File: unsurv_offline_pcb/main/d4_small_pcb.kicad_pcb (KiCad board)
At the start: 4 copper layers, 32 x 45 mm, 51 parts, among them Q1 UMH3N, Q2 Q_PMOS_GSD, U1 TTGO-Micro32-ESP32, U2 MCP73831-2-OT, U3 CAM-M8C-0-10, U4 AP2112K-3.3, U5 CH340G, U6 RF430CL330H, U7 BMA400-I2C

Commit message: d4 case updates
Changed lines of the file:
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@@
     (uvia_drill 0.1)
+  )
+  (module unsurv_offline_pcb_footprints:BMA400 (layer F.Cu)
+    (at 44.9 50.5)
+    (fp_text reference U7 (at 2.9 0) (layer F.SilkS)
+      (effects (font (size 0.4 0.4) (thickness 0.08)))
+    )
+    (fp_text value BMA400-I2C (at 0 2.1) (layer F.Fab)
+      (effects (font (size 1 1) (thickness 0.15)))
+    )
+    (fp_circle (center -1.55 -1.07) (end -1.64 -0.96) (layer F.SilkS) (width 0.12))
+    (fp_line (start -1 1) (end 1 1) (layer F.SilkS) (width 0.12))
+    (fp_line (start -1 -1) (end -1 1) (layer F.SilkS) (width 0.12))
+    (fp_line (start 1 -1) (end -1 -1) (layer F.SilkS) (width 0.12))
+    (fp_line (start 1 1) (end 1 -1) (layer F.SilkS) (width 0.12))
+    (pad 11 smd rect (at 0.25 -0.9 270) (size 0.6 0.28) (layers F.Cu F.Paste F.Mask)
+      (net 34 "Net-(U7-Pad11)"))
+    (pad 12 smd rect (at -0.25 -0.9 270) (size 0.6 0.28) (layers F.Cu F.Paste F.Mask)
+      (net 23 SCL))
+    (pad 10 smd rect (at 0.9 -0.75 180) (size 0.6 0.28) (layers F.Cu F.Paste F.Mask)
+      (net 7 +3V3))
+    (pad 9 smd rect (at 0.9 -0.25 180) (size 0.6 0.28) (layers F.Cu F.Paste F.Mask)
+      (net 4 GND))
+    (pad 8 smd rect (at 0.9 0.25 180) (size 0.6 0.28) (layers F.Cu F.Paste F.Mask)
+      (net 4 GND))
+    (pad 7 smd rect (at 0.9 0.75 180) (size 0.6 0.28) (layers F.Cu F.Paste F.Mask)
+      (net 7 +3V3))
+    (pad 6 smd rect (at 0.25 0.9 90) (size 0.6 0.28) (layers F.Cu F.Paste F.Mask)
+      (net 27 ACC_INT2))
+    (pad 5 smd rect (at -0.25 0.9 90) (size 0.6 0.28) (layers F.Cu F.Paste F.Mask)
+      (net 26 ACC_INT1))
+    (pad 4 smd rect (at -0.9 0.75) (size 0.6 0.28) (layers F.Cu F.Paste F.Mask)
+      (net 81 "Net-(U7-Pad4)"))
+    (pad 3 smd rect (at -0.9 0.25) (size 0.6 0.28) (layers F.Cu F.Paste F.Mask)
+      (net 7 +3V3))
+    (pad 2 smd rect (at -0.9 -0.25) (size 0.6 0.28) (layers F.Cu F.Paste F.Mask)
+      (net 22 SDA))
+    (pad 1 smd rect (at -0.9 -0.75) (size 0.6 0.28) (layers F.Cu F.Paste F.Mask)
+      (net 4 GND))
   )
   (module unsurv_offline_pcb_footprints:TF-SMD_TF-101B (layer F.Cu)
@@
     )
   )
-  (module unsurv_offline_pcb_footprints:BMA400 (layer F.Cu)
-    (at 44.9 50.5)
-    (fp_text reference U7 (at 2.9 0) (layer F.SilkS)
-      (effects (font (size 0.4 0.4) (thickness 0.08)))
-    )
-    (fp_text value BMA400-I2C (at 0 2.1) (layer F.Fab)
-      (effects (font (size 1 1) (thickness 0.15)))
-    )
-    (fp_line (start 1 1) (end 1 -1) (layer F.SilkS) (width 0.12))
-    (fp_line (start 1 -1) (end -1 -1) (layer F.SilkS) (width 0.12))
-    (fp_line (start -1 -1) (end -1 1) (layer F.SilkS) (width 0.12))
-    (fp_line (start -1 1) (end 1 1) (layer F.SilkS) (width 0.12))
-    (pad 1 smd rect (at -0.9 -0.75) (size 0.6 0.28) (layers F.Cu F.Paste F.Mask)
-      (net 4 GND))
-    (pad 2 smd rect (at -0.9 -0.25) (size 0.6 0.28) (layers F.Cu F.Paste F.Mask)
-      (net 22 SDA))
-    (pad 3 smd rect (at -0.9 0.25) (size 0.6 0.28) (layers F.Cu F.Paste F.Mask)
-      (net 7 +3V3))
-    (pad 4 smd rect (at -0.9 0.75) (size 0.6 0.28) (layers F.Cu F.Paste F.Mask)
-      (net 81 "Net-(U7-Pad4)"))
-    (pad 5 smd rect (at -0.25 0.9 90) (size 0.6 0.28) (layers F.Cu F.Paste F.Mask)
-      (net 26 ACC_INT1))
-    (pad 6 smd rect (at 0.25 0.9 90) (size 0.6 0.28) (layers F.Cu F.Paste F.Mask)
-      (net 27 ACC_INT2))
-    (pad 7 smd rect (at 0.9 0.75 180) (size 0.6 0.28) (layers F.Cu F.Paste F.Mask)
-      (net 7 +3V3))
-    (pad 8 smd rect (at 0.9 0.25 180) (size 0.6 0.28) (layers F.Cu F.Paste F.Mask)
-      (net 4 GND))
-    (pad 9 smd rect (at 0.9 -0.25 180) (size 0.6 0.28) (layers F.Cu F.Paste F.Mask)
-      (net 4 GND))
-    (pad 10 smd rect (at 0.9 -0.75 180) (size 0.6 0.28) (layers F.Cu F.Paste F.Mask)
-      (net 7 +3V3))
-    (pad 12 smd rect (at -0.25 -0.9 270) (size 0.6 0.28) (layers F.Cu F.Paste F.Mask)
-      (net 23 SCL))
-    (pad 11 smd rect (at 0.25 -0.9 270) (size 0.6 0.28) (layers F.Cu F.Paste F.Mask)
-      (net 34 "Net-(U7-Pad11)"))
-  )
   (module Package_SO:SOIC-16_3.9x9.9mm_P1.27mm (layer F.Cu)

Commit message: small updates to PCB and case
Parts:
- removed JP2: SolderJumper_2_Open, Jumper:SolderJumper-2_P1.3mm_Open_RoundedPad1.0x1.5mm
- C3: value 2.2yF -> 4.7yF
- moved S2 0.20 mm to (34.7, 55.7)
- renumbered + to BATT+1, - to BATT-1
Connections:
- R4 pad 1: Net-(JP2-Pad1) -> +3V3
- R5 pad 1: Net-(JP2-Pad1) -> +3V3
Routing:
- net Net-(JP2-Pad1): track 6.34 -> 0.00 mm, vias 1 -> 0
- net +3V3: track 58.9 -> 60.3 mm
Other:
- board text removed: "I2C 3.3k Pullups"

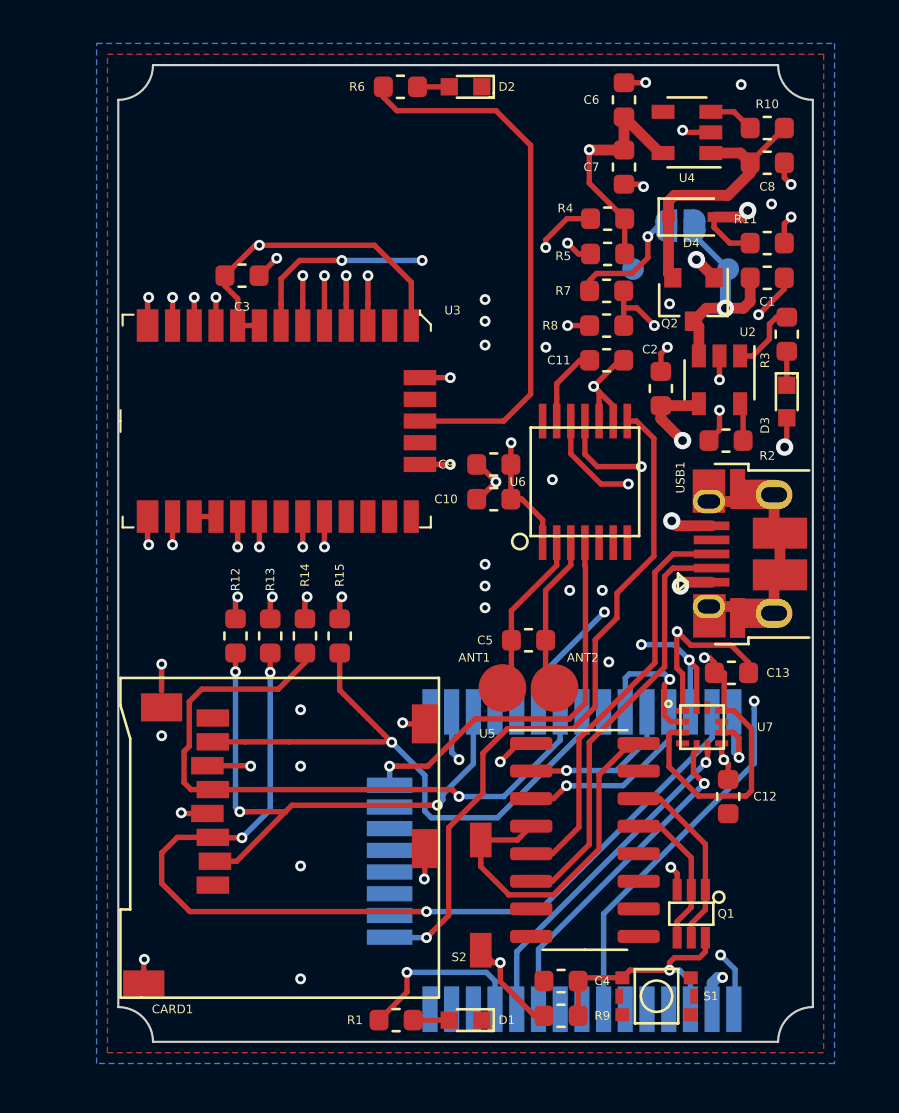
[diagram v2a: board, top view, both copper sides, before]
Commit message: added expansion and JST
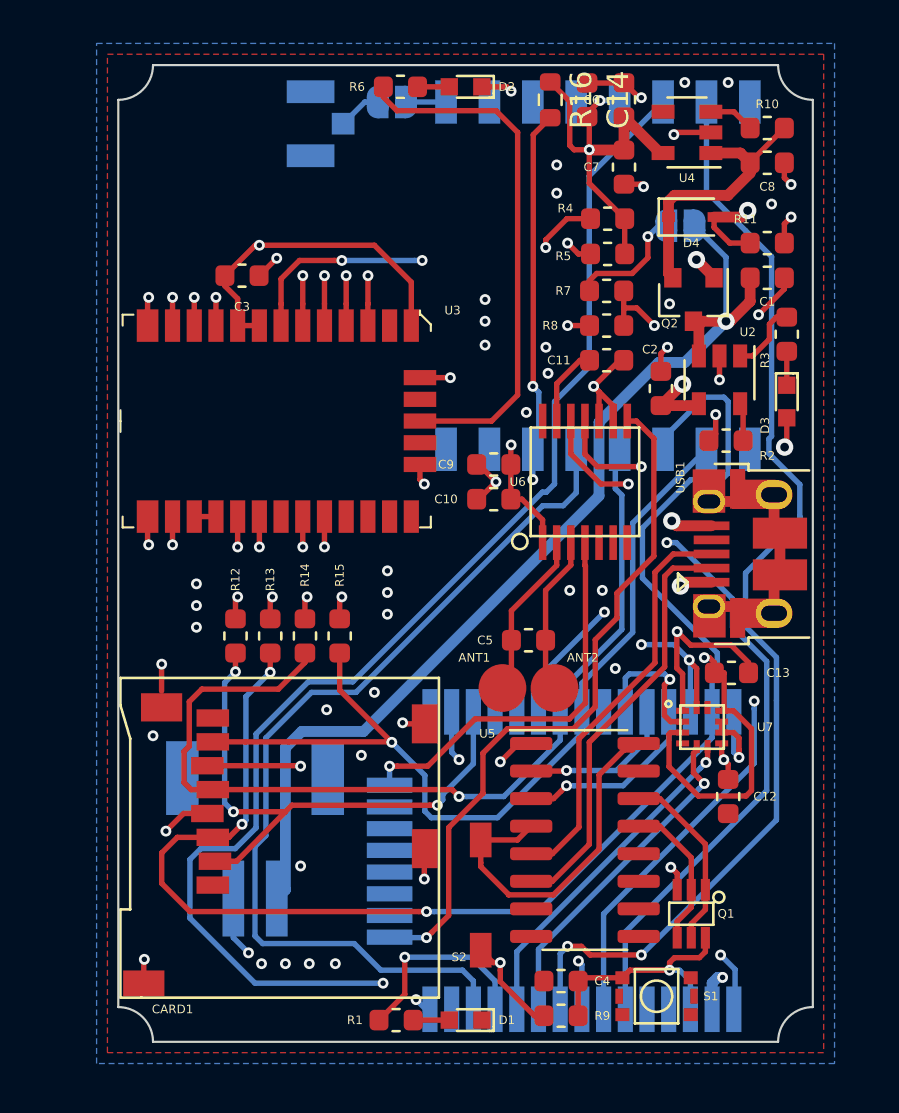
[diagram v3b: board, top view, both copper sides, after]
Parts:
- removed BATT+1: +, TestPoint:TestPoint_Pad_D1.0mm
- removed BATT-1: -, TestPoint:TestPoint_Pad_D1.0mm
- added C14: 4.7yF, Capacitor_SMD:C_0603_1608Metric, F.Cu at (39.6, 21.6)
- added J1: U_FL-R-SMT-1_10_, digikey-footprints:Coax_Conn_U.FL, B.Cu at (26.9, 22.7)
- added J2: S2B-PH-SM4-TB_LF__SN_, digikey-footprints:PinHeader_2x1mm_P2mm_SMD_RA, B.Cu at (24.3, 58.4)
- added JP2: SolderJumper_2_Open, Jumper:SolderJumper-2_P1.3mm_Open_RoundedPad1.0x1.5mm, B.Cu at (30.6, 21.7)
- added R16: 10k, Resistor_SMD:R_0603_1608Metric, F.Cu at (37.9, 21.6)
- added U8: RFM95W-868S2, RF_Module:HOPERF_RFM9XW_SMD, B.Cu at (40.1, 29.7)
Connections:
- CARD1 pad 1: Net-(CARD1-Pad1) -> unconnected-(CARD1-Pad1)
- CARD1 pad 8: Net-(CARD1-Pad8) -> unconnected-(CARD1-Pad8)
- S1 pad 2: Net-(S1-Pad2) -> unconnected-(S1-Pad2)
- U1 pad 13: Net-(U1-Pad13) -> 14
- U1 pad 14: Net-(U1-Pad14) -> unconnected-(U1-Pad14)
- U1 pad 17: Net-(U1-Pad17) -> unconnected-(U1-Pad17)
- U1 pad 18: Net-(U1-Pad18) -> unconnected-(U1-Pad18)
- U1 pad 19: Net-(U1-Pad19) -> unconnected-(U1-Pad19)
- U1 pad 20: Net-(U1-Pad20) -> unconnected-(U1-Pad20)
- U1 pad 21: Net-(U1-Pad21) -> unconnected-(U1-Pad21)
- U1 pad 22: Net-(U1-Pad22) -> unconnected-(U1-Pad22)
- U1 pad 24: Net-(U1-Pad24) -> unconnected-(U1-Pad24)
- U1 pad 27: Net-(U1-Pad27) -> unconnected-(U1-Pad27)
- U1 pad 28: Net-(U1-Pad28) -> unconnected-(U1-Pad28)
- U1 pad 32: Net-(U1-Pad32) -> unconnected-(U1-Pad32)
- U1 pad 4: Net-(U1-Pad4) -> unconnected-(U1-Pad4)
- U1 pad 5: Net-(U1-Pad5) -> unconnected-(U1-Pad5)
- U1 pad 6: Net-(U1-Pad6) -> 34
- U1 pad 8: Net-(U1-Pad8) -> 32
- U1 pad 9: Net-(U1-Pad9) -> 33
- U3 pad 2: Net-(U3-Pad2) -> unconnected-(U3-Pad2)
- U3 pad 20: Net-(U3-Pad20) -> unconnected-(U3-Pad20)
- U3 pad 23: Net-(U3-Pad23) -> unconnected-(U3-Pad23)
- U3 pad 24: Net-(U3-Pad24) -> unconnected-(U3-Pad24)
- U3 pad 25: Net-(U3-Pad25) -> unconnected-(U3-Pad25)
- U3 pad 26: Net-(U3-Pad26) -> unconnected-(U3-Pad26)
- U3 pad 28: Net-(U3-Pad28) -> unconnected-(U3-Pad28)
- U3 pad 30: Net-(U3-Pad30) -> unconnected-(U3-Pad30)
- U4 pad 4: Net-(U4-Pad4) -> unconnected-(U4-Pad4)
- U5 pad 10: Net-(U5-Pad10) -> unconnected-(U5-Pad10)
- U5 pad 11: Net-(U5-Pad11) -> unconnected-(U5-Pad11)
- U5 pad 12: Net-(U5-Pad12) -> unconnected-(U5-Pad12)
- U5 pad 15: Net-(U5-Pad15) -> unconnected-(U5-Pad15)
- U5 pad 7: Net-(U5-Pad7) -> unconnected-(U5-Pad7)
- U5 pad 8: Net-(U5-Pad8) -> unconnected-(U5-Pad8)
- U5 pad 9: Net-(U5-Pad9) -> unconnected-(U5-Pad9)
- U6 pad 5: Net-(U6-Pad5) -> unconnected-(U6-Pad5)
- U6 pad 6: Net-(U6-Pad6) -> unconnected-(U6-Pad6)
- U6 pad 7: Net-(U6-Pad7) -> unconnected-(U6-Pad7)
- U7 pad 11: Net-(U7-Pad11) -> unconnected-(U7-Pad11)
- U7 pad 4: Net-(U7-Pad4) -> unconnected-(U7-Pad4)
- USB1 pad 4: Net-(USB1-Pad4) -> unconnected-(USB1-Pad4)
- USB1 pad 6: Net-(USB1-Pad6) -> unconnected-(USB1-Pad6)
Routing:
- net 32: track 0.00 -> 70.7 mm, vias 0 -> 2
- net 33: track 0.00 -> 52.0 mm, vias 0 -> 2
- net 34: track 0.00 -> 51.0 mm, vias 0 -> 3
- net 14: track 0.00 -> 42.5 mm
- net +BATT: track 10.3 -> 48.3 mm
- net 23: track 44.9 -> 67.2 mm
- net 19: track 27.1 -> 41.6 mm
- net 18: track 30.3 -> 43.8 mm
- net unconnected-(USB1-Pad6): track 0.00 -> 11.9 mm
- net Net-(USB1-Pad6): track 11.9 -> 0.00 mm
- net GND: track 69.3 -> 77.8 mm, vias 56 -> 70
- net +3V3: track 60.3 -> 68.6 mm, vias 12 -> 13
- net Net-(J1-Pad2): track 0.00 -> 2.00 mm
- net ANT: track 0.00 -> 1.85 mm
- net 27: track 8.26 -> 9.31 mm
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- added copper zone on In2.Cu, net +3V3
- added copper zone on In2.Cu, net +5V
- added copper zone on In1.Cu, net GND
- removed copper zone on VCC, net +3V3
- removed copper zone on VCC, net +5V
- removed copper zone on GND, net GND
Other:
- net class AISLER 4 layer removed
- net class Default removed

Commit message: changed voltage divider routing
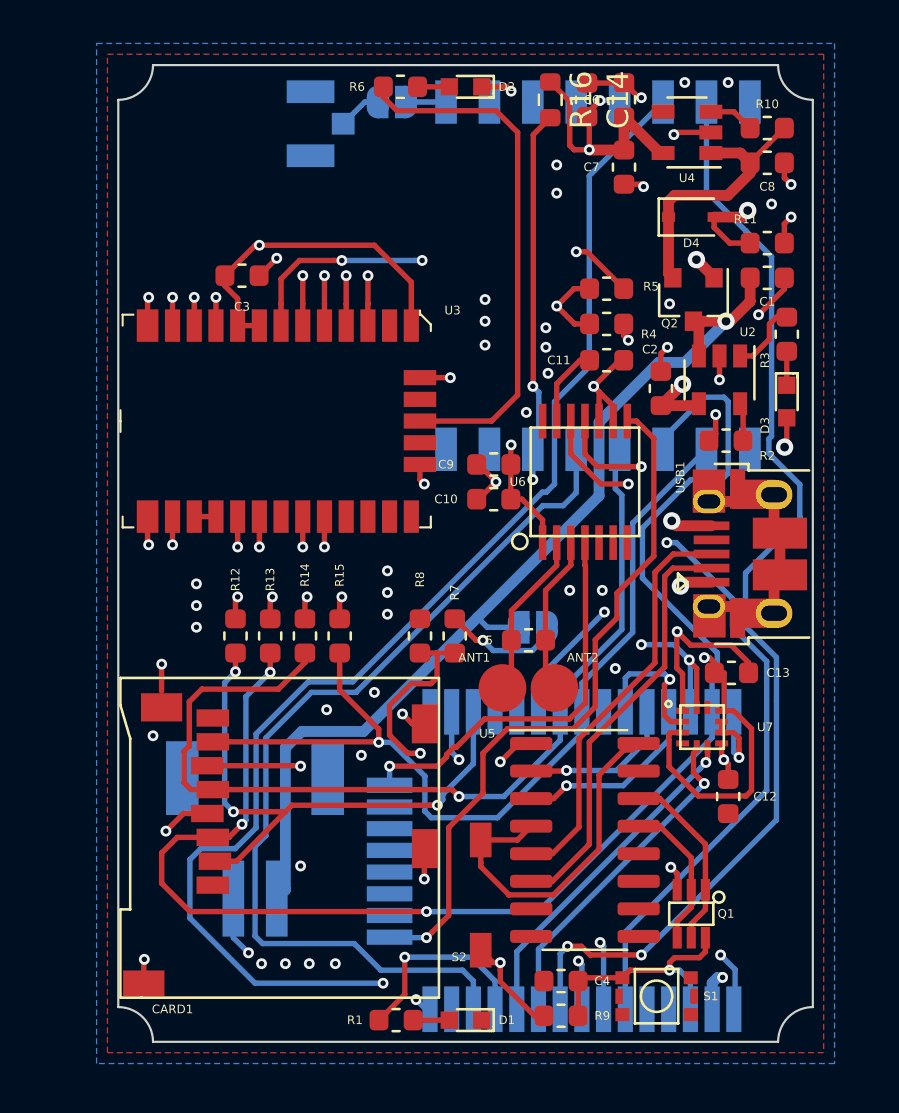
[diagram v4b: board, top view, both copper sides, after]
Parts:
- moved JP1 19.7 mm to (37.1, 45.9), turned to 0 degrees
- moved R7 17.4 mm to (33.5, 46.3), turned to -90 degrees
- moved R8 16.7 mm to (31.9, 46.3), turned to 90 degrees
- moved R4 4.85 mm to (40.5, 31.9), turned to 0 degrees
- moved R5 1.60 mm to (40.5, 30.3), turned to 0 degrees
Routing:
- net 35: track 39.6 -> 25.6 mm
- net +BATT: track 48.3 -> 45.4 mm
- net SDA: track 47.7 -> 45.7 mm
- net +3V3: track 68.6 -> 66.8 mm, vias 13 -> 14
- net SCL: track 48.2 -> 49.9 mm
- net GND: track 77.8 -> 76.9 mm

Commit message: 3v3 plane cleanup
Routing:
- net 0: track 15.3 -> 20.2 mm
- net GND: track 76.9 -> 78.6 mm

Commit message: v 0.3.1 PCB
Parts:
- moved R4 1.29 mm to (39.6, 30.9), turned to 90 degrees
- moved R5 1.11 mm to (41.4, 30.9), turned to 90 degrees
- moved J2 0.95 mm to (24.3, 59.4)
- moved Q1 0.64 mm to (44.9, 58.7)
- moved J1 0.30 mm to (26.6, 22.7)
- moved JP2 0.20 mm to (30.4, 21.7)
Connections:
- U6 pad 8: 13 -> 32
- U8 pad 14: 32 -> 13
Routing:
- net 13: track 32.4 -> 47.7 mm, vias 1 -> 2
- net 32: track 70.7 -> 62.0 mm, vias 2 -> 3
- net +3V3: track 66.8 -> 68.8 mm
- net GND: track 78.6 -> 77.3 mm, vias 70 -> 68
- net +BATT: track 45.4 -> 46.4 mm
- net 33: track 52.0 -> 51.3 mm
- net 0: track 20.2 -> 20.8 mm
- net RESET: track 11.3 -> 11.9 mm
- net 14: track 42.5 -> 43.1 mm
- net 5: vias 3 -> 4
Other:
- board text added: "unsurv offline v0.3.1 pre production"

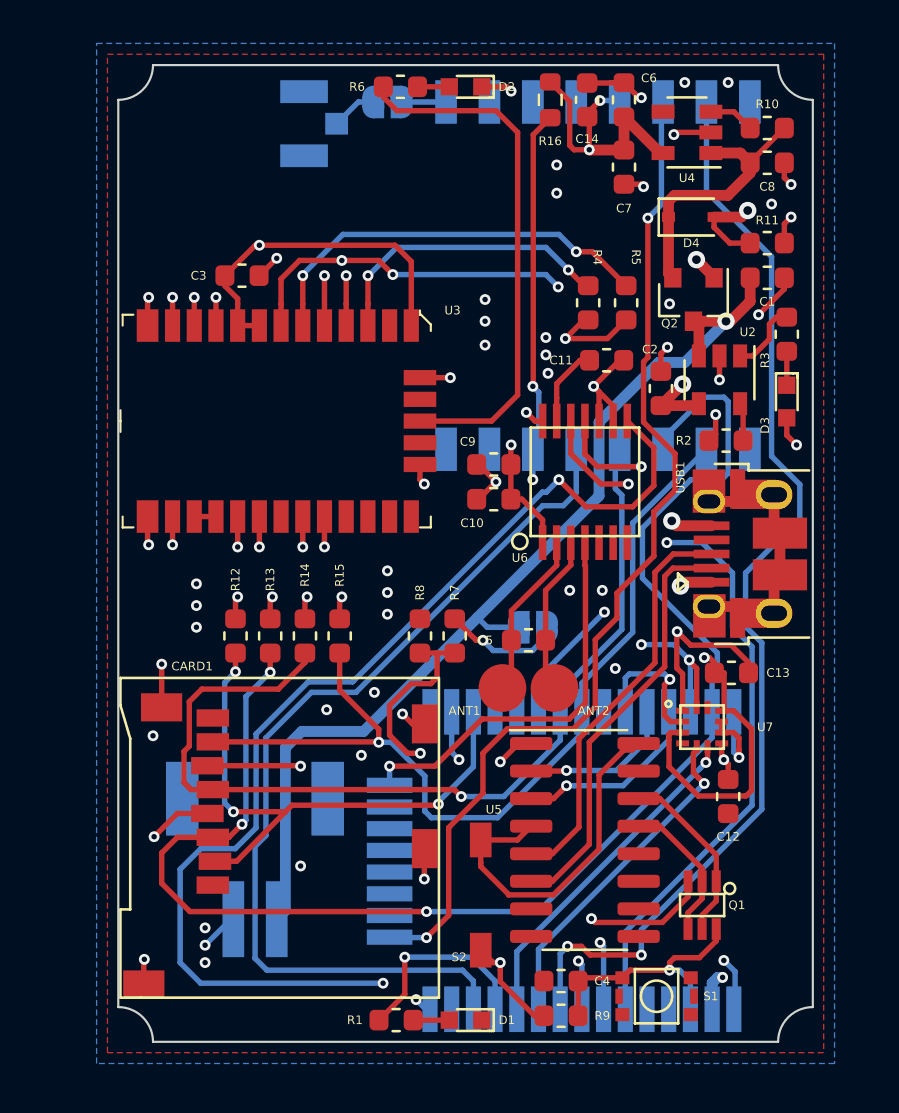
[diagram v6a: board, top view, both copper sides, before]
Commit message: added new 3D case + PCB rework
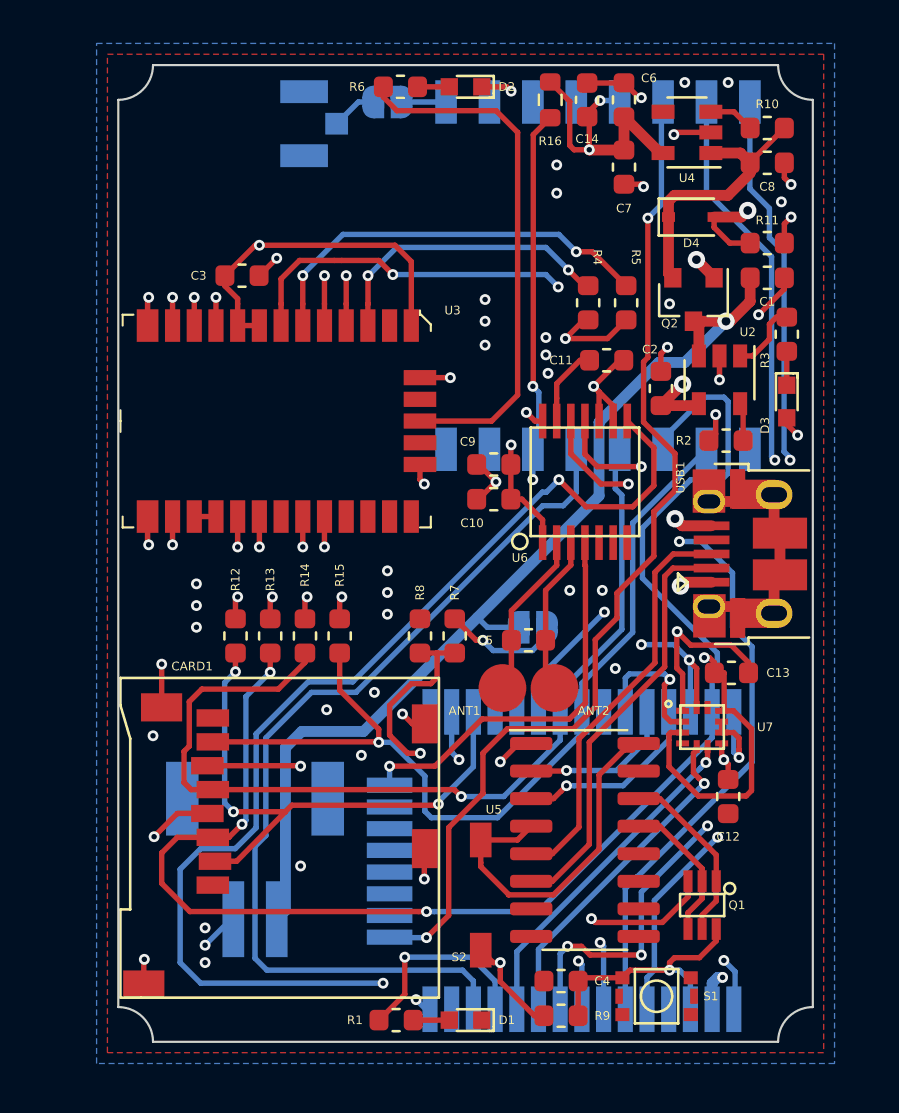
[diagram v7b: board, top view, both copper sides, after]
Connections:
- U1 pad 5: unconnected-(U1-Pad5) -> 39
- U8 pad 16: unconnected-(U8-Pad16) -> 39
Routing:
- net 39: track 0.00 -> 46.7 mm, vias 0 -> 2
- net +5V: track 11.4 -> 10.9 mm
- net 33: track 51.3 -> 51.0 mm, vias 2 -> 4
- net 5: vias 4 -> 3
